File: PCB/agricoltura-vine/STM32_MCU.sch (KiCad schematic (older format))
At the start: 28 parts

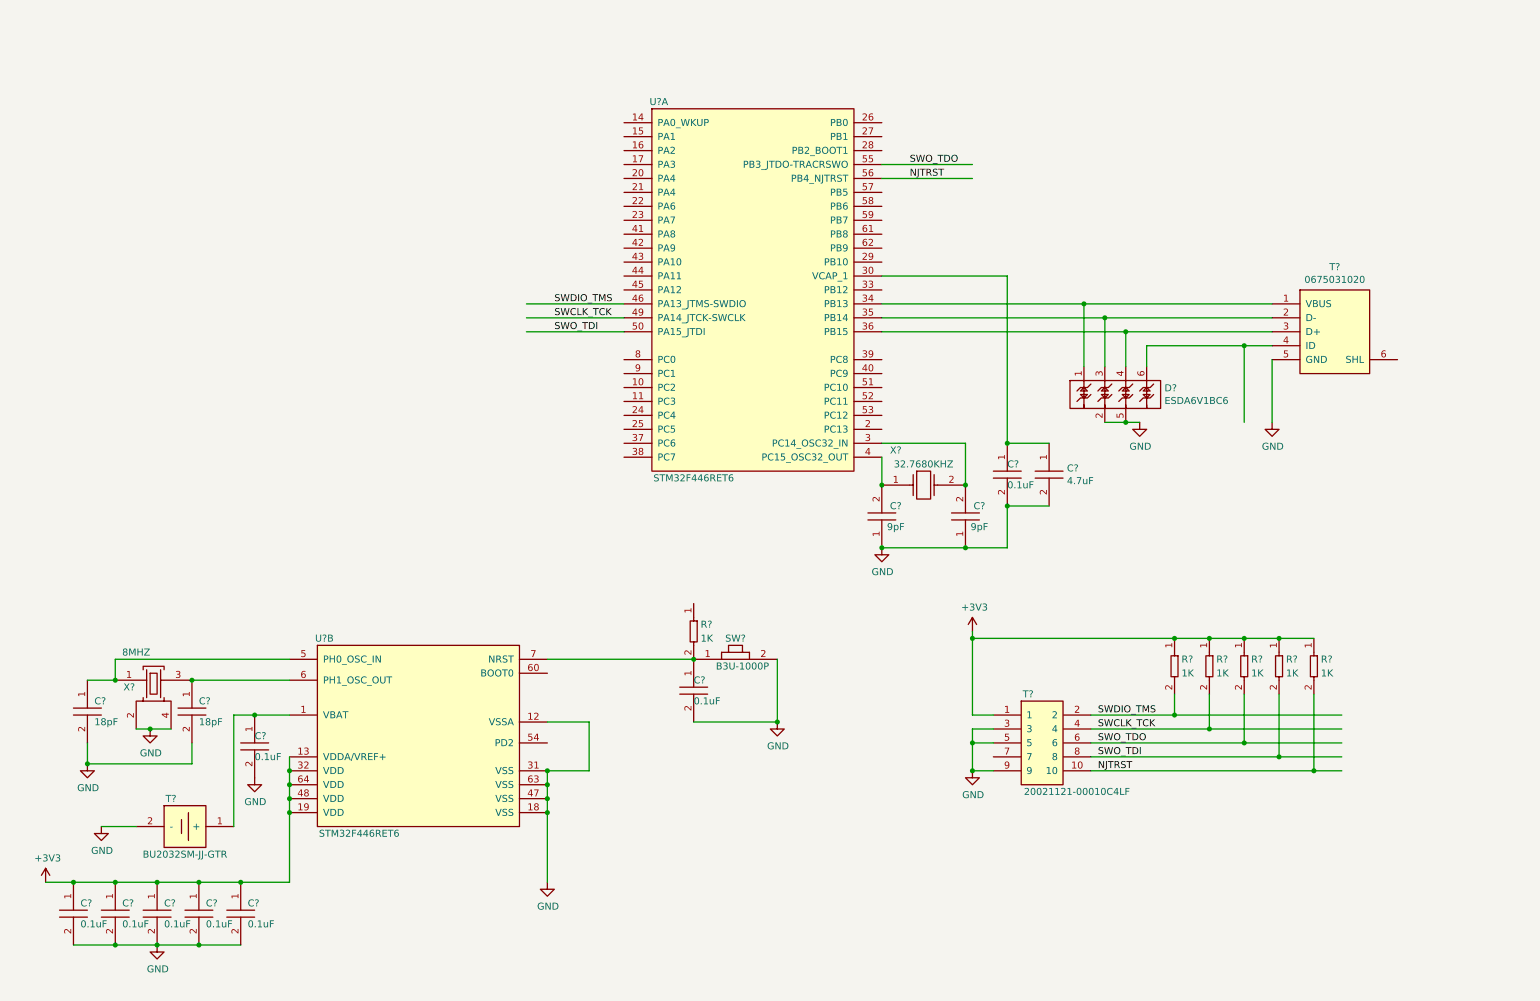
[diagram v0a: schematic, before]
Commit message: Schematic process
scheamtics laid out for all board subsyhstems, connecting MCU to subsystems still in progress, power yet to be designed.
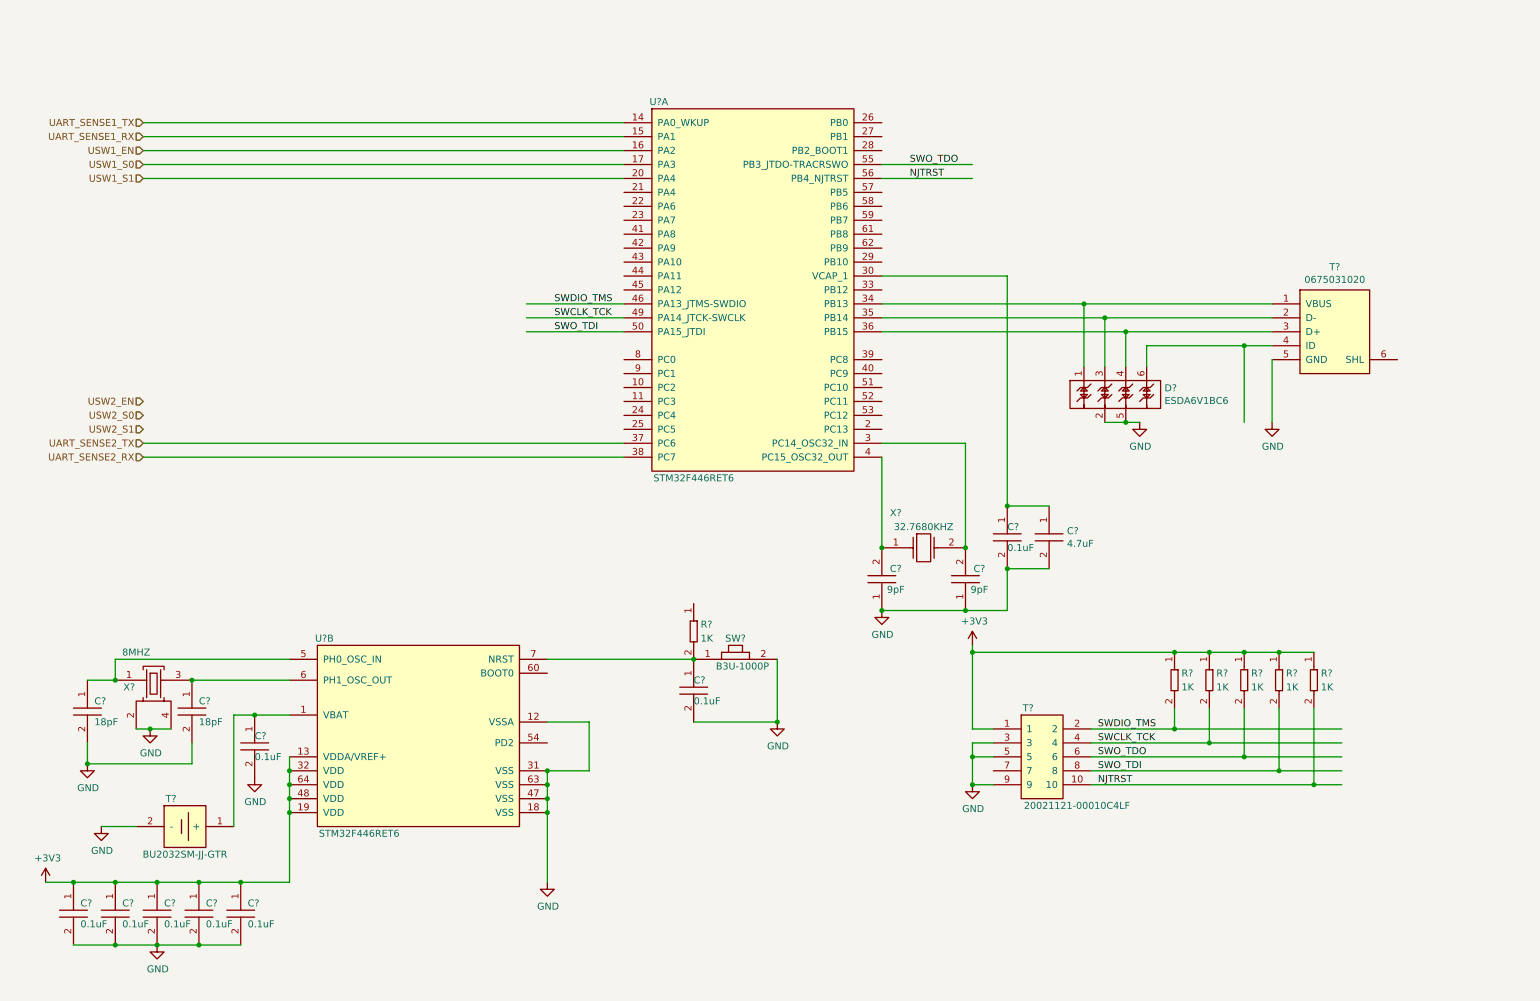
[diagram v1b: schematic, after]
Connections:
- net labels added: UART_SENSE1_RX, UART_SENSE1_TX, UART_SENSE2_RX, UART_SENSE2_TX, USW1_EN, USW1_S0, USW1_S1, USW2_EN, USW2_S0, USW2_S1
- wire segments 97 -> 104
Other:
- moved on the sheet: C?, R?, T?, X?

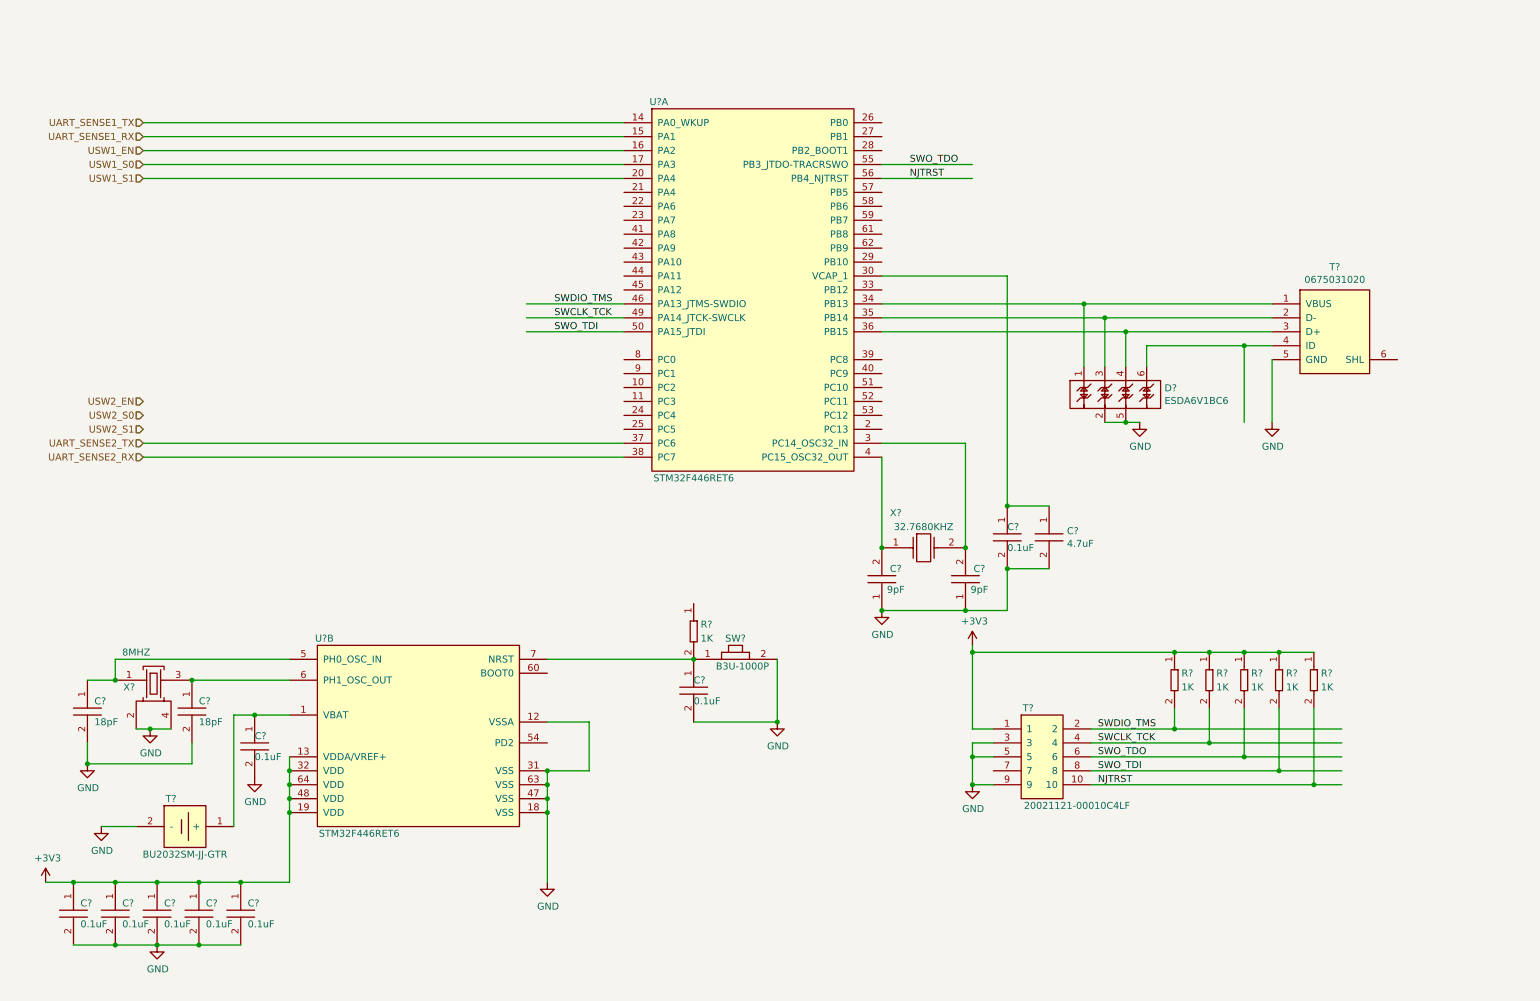
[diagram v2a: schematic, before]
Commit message: Power supplies
Both power supplies redsigned around new ICs for 2A of each voltage, since we have no idea how much current peripherals will be using.
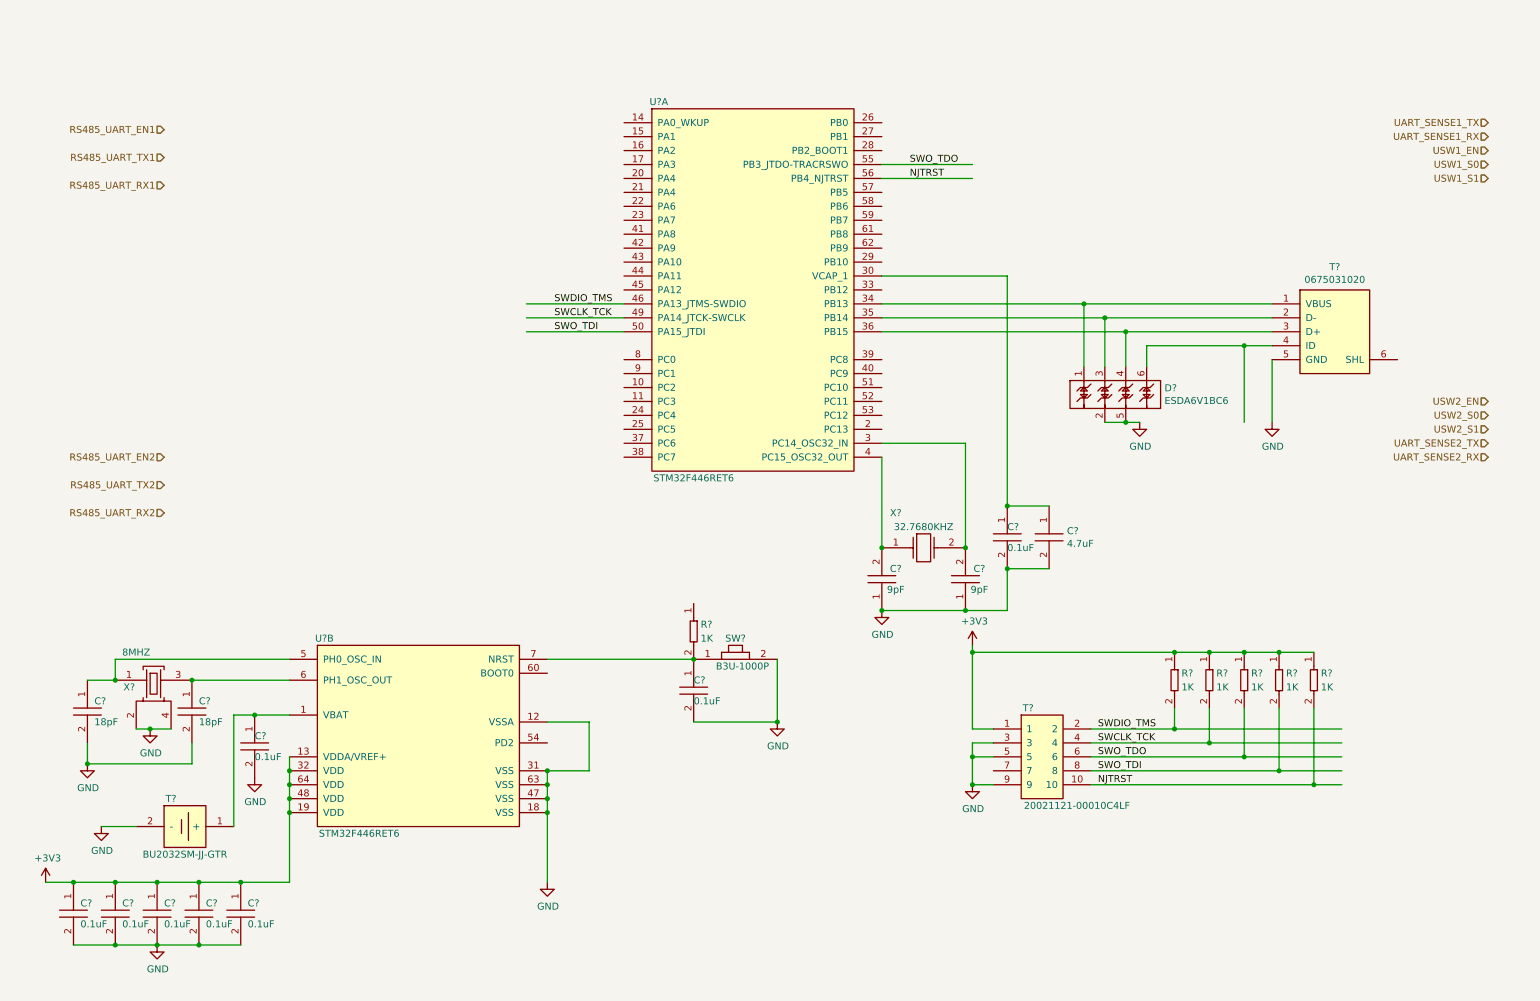
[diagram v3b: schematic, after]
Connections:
- net labels added: RS485_UART_EN1, RS485_UART_EN2, RS485_UART_RX1, RS485_UART_RX2, RS485_UART_TX1, RS485_UART_TX2
- wire segments 104 -> 97
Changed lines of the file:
@@
 	8400 3700 8250 3700
 Connection ~ 7550 4300
-Text HLabel 1350 1550 0    50   Input ~ 0
+Text HLabel 11000 1550 0    50   Input ~ 0
 UART_SENSE1_TX
-Text HLabel 1350 1650 0    50   Input ~ 0
+Text HLabel 11000 1650 0    50   Input ~ 0
 UART_SENSE1_RX
-Text HLabel 1350 3850 0    50   Input ~ 0
+Text HLabel 11000 3850 0    50   Input ~ 0
 UART_SENSE2_TX
-Text HLabel 1350 3950 0    50   Input ~ 0
+Text HLabel 11000 3950 0    50   Input ~ 0
 UART_SENSE2_RX
-Text HLabel 1350 1950 0    50   Input ~ 0
+Text HLabel 11000 1950 0    50   Input ~ 0
 USW1_S1
-Text HLabel 1350 1850 0    50   Input ~ 0
+Text HLabel 11000 1850 0    50   Input ~ 0
 USW1_S0
-Text HLabel 1350 1750 0    50   Input ~ 0
+Text HLabel 11000 1750 0    50   Input ~ 0
 USW1_EN
-Text HLabel 1350 3750 0    50   Input ~ 0
+Text HLabel 11000 3750 0    50   Input ~ 0
 USW2_S1
-Text HLabel 1350 3650 0    50   Input ~ 0
+Text HLabel 11000 3650 0    50   Input ~ 0
 USW2_S0
-Text HLabel 1350 3550 0    50   Input ~ 0
+Text HLabel 11000 3550 0    50   Input ~ 0
 USW2_EN
-Wire Wire Line
-	4800 1550 1350 1550
-Wire Wire Line
-	4800 1650 1350 1650
-Wire Wire Line
-	4800 1750 1350 1750
-Wire Wire Line
-	1350 1850 4800 1850
-Wire Wire Line
-	4800 1950 1350 1950
-Wire Wire Line
-	4800 3850 1350 3850
-Wire Wire Line
-	4800 3950 1350 3950
+Text HLabel 1500 1600 0    50   Input ~ 0
+RS485_UART_EN1
+Text HLabel 1500 1800 0    50   Input ~ 0
+RS485_UART_TX1
+Text HLabel 1500 2000 0    50   Input ~ 0
+RS485_UART_RX1
+Text HLabel 1500 3950 0    50   Input ~ 0
+RS485_UART_EN2
+Text HLabel 1500 4150 0    50   Input ~ 0
+RS485_UART_TX2
+Text HLabel 1500 4350 0    50   Input ~ 0
+RS485_UART_RX2
 $EndSCHEMATC

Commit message: Schematic Pass 1
All subsystem schematics are completed in their first pass, some features scaled back to make design more practical.
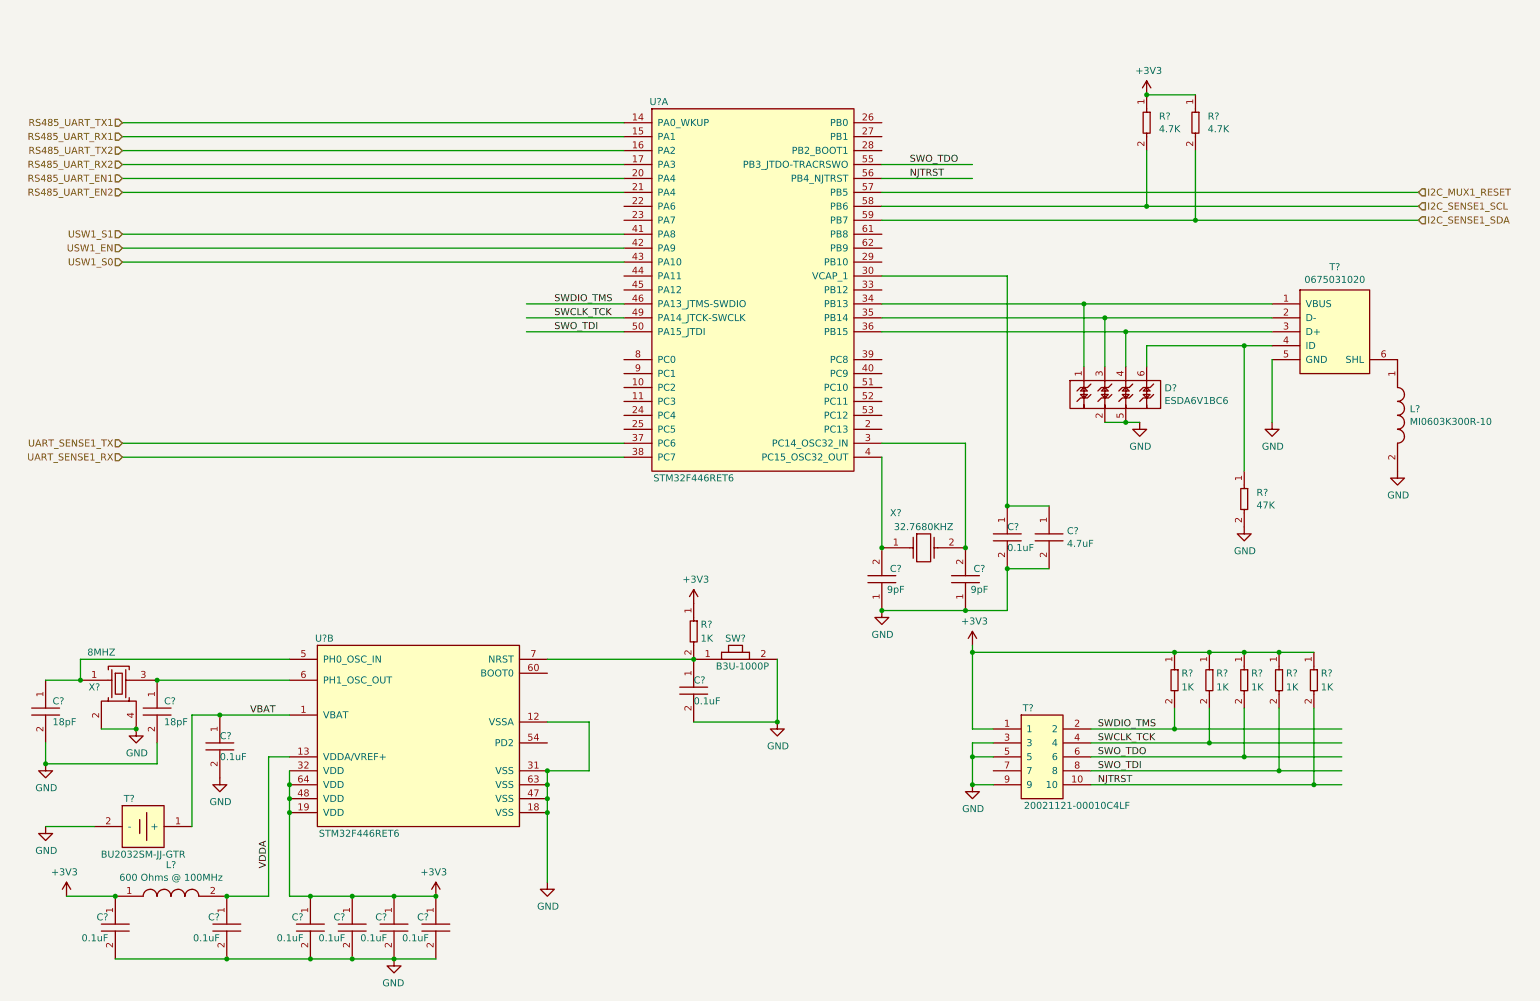
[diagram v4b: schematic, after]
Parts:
- added C?: C0402C104K9PACTU, AVR-KiCAD-Lib-Resistors:R0402, symbol AVR-KiCAD-Lib-Capacitors:C0402C104K9PACTU
- added L?: BLM15HG601SN1D, AVR-KiCAD-Lib-Inductors:BLM15HG601SN1D, symbol AVR-KiCAD-Lib-Inductors:BLM15HG601SN1D
- added L?: MI0603K300R-10, AVR-KiCAD-Lib-Inductors:MI0603K300R-10, symbol AVR-KiCAD-Lib-Inductors:MI0603K300R-10
- added R? (x2): RC0402FR-074K7L, AVR-KiCAD-Lib-Resistors:R0402, symbol AVR-KiCAD-Lib-Resistors:RC0402FR-074K7L
- added R?: RC0603FR-0747KL, AVR-KiCAD-Lib-Resistors:R0603, symbol AVR-KiCAD-Lib-Resistors:RC0603FR-0747KL
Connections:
- net labels added: I2C_MUX1_RESET, I2C_SENSE1_SCL, I2C_SENSE1_SDA, VBAT, VDDA
- net labels removed: UART_SENSE2_RX, UART_SENSE2_TX, USW2_EN, USW2_S0, USW2_S1
- wire segments 97 -> 117
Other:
- moved on the sheet: C?, T?, X?

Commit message: Board
Board shape defined, though subject to change. Schematic anotated and parts exported to board.
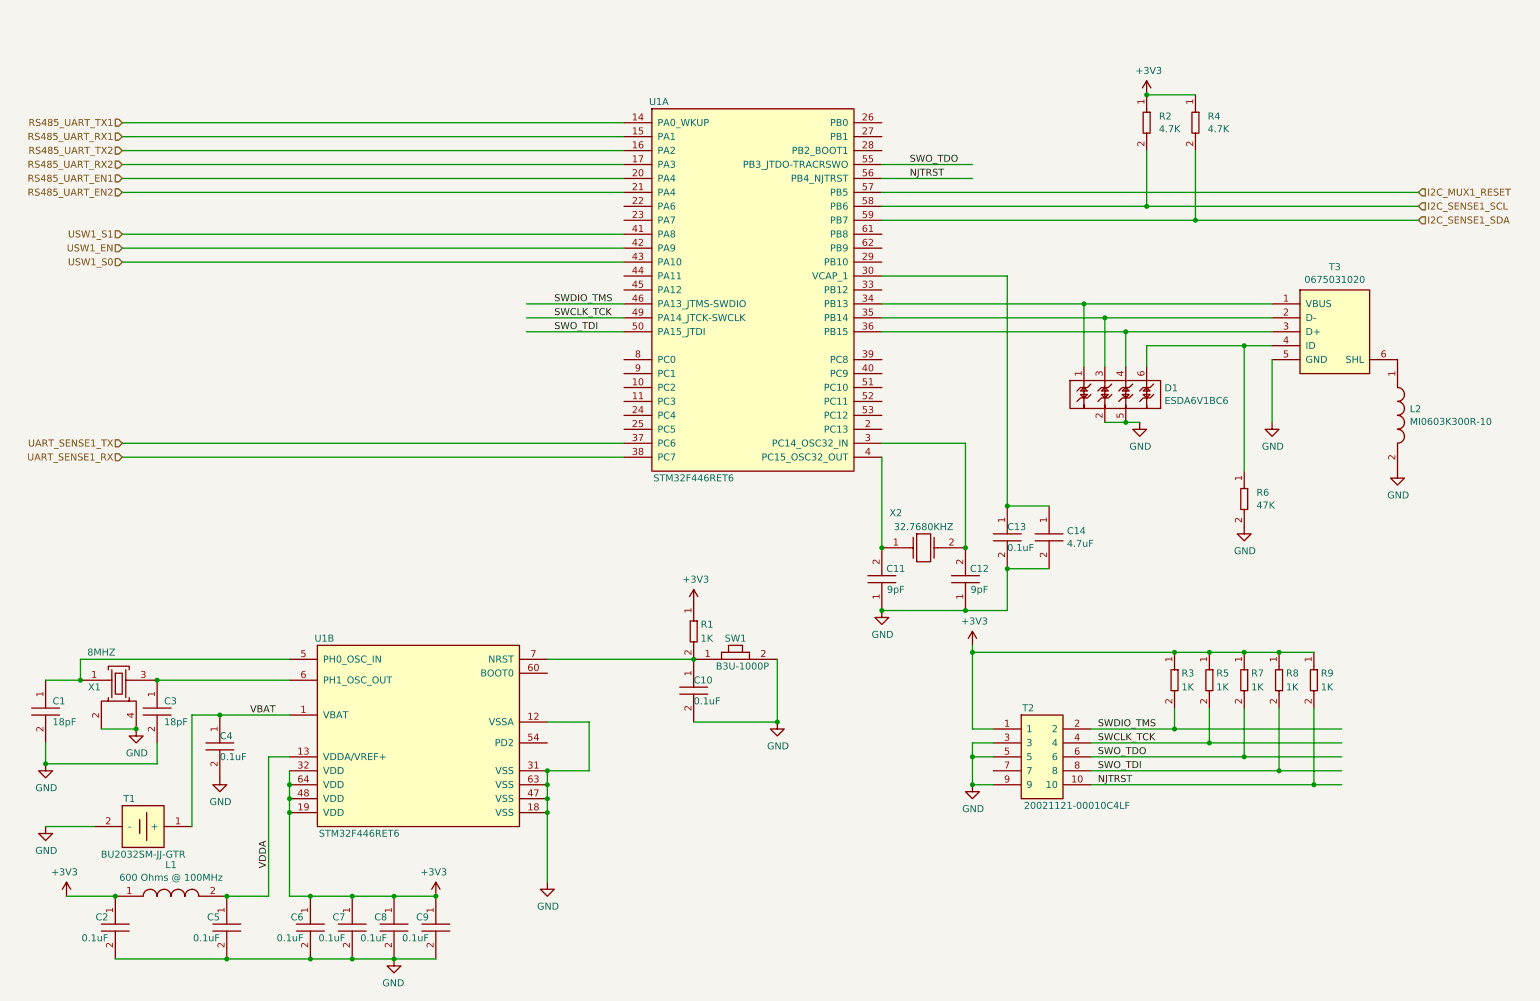
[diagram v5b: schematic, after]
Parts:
- T1: renamed from T?; footprint AVR-KiCAD-Lib-Connectors:BU2032SM-JJ-GTR -> AVR-KiCAD-Lib-Battery-Holders:BU2032SM-JJ-GTR
- gave numbers to parts that had none: 32
